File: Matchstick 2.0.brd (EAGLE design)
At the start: 73 x 38 mm, 13 parts, among them IC1 74HCT125D, J1 694106301002, J2 TARGET, J3 691241510006, J4 691241510006, U1 M5STAMP PICO

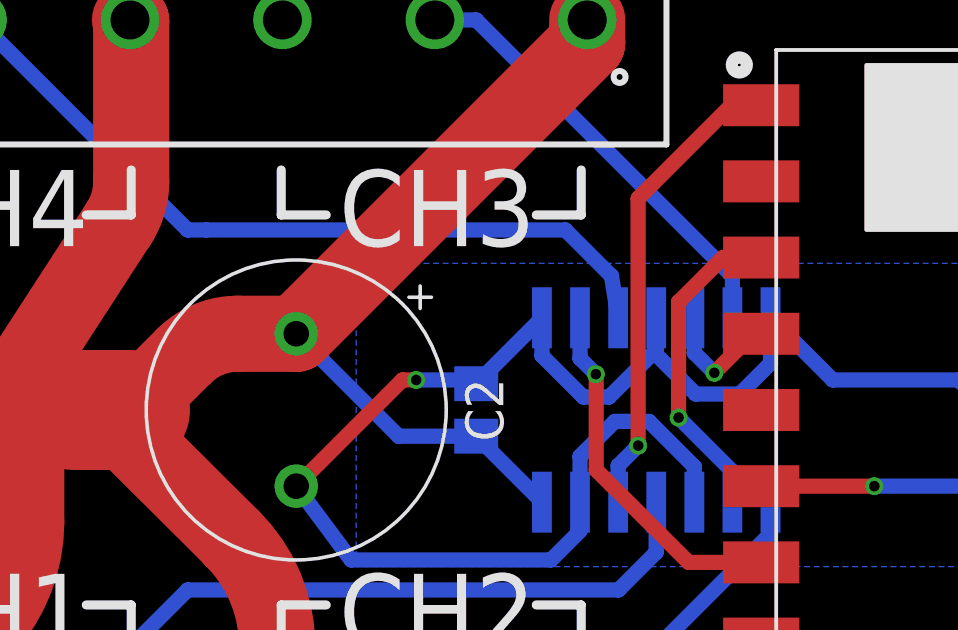
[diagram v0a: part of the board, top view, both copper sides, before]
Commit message: fix few alignment issues
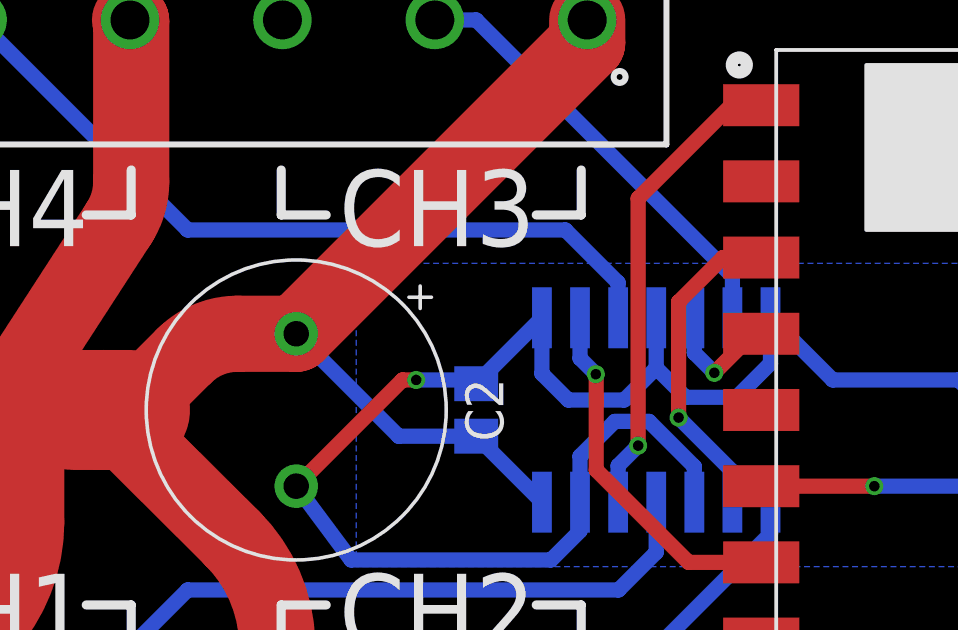
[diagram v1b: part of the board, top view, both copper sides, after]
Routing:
- net GND: track 67.9 -> 67.3 mm
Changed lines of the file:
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@@
 <grid distance="1" unitdist="mm" unit="mm" style="lines" multiple="1" display="yes" altdistance="0.1" altunitdist="mm" altunit="mm"/>
 <layers>
-<layer number="1" name="Top" color="4" fill="1" visible="no" active="yes"/>
+<layer number="1" name="Top" color="4" fill="1" visible="yes" active="yes"/>
 <layer number="16" name="Bottom" color="1" fill="1" visible="yes" active="yes"/>
 <layer number="17" name="Pads" color="2" fill="1" visible="yes" active="yes"/>
@@
 <layer number="19" name="Unrouted" color="6" fill="1" visible="yes" active="yes"/>
 <layer number="20" name="Dimension" color="24" fill="1" visible="yes" active="yes"/>
-<layer number="21" name="tPlace" color="7" fill="1" visible="no" active="yes"/>
+<layer number="21" name="tPlace" color="7" fill="1" visible="yes" active="yes"/>
 <layer number="22" name="bPlace" color="7" fill="1" visible="yes" active="yes"/>
-<layer number="23" name="tOrigins" color="15" fill="1" visible="no" active="yes"/>
+<layer number="23" name="tOrigins" color="15" fill="1" visible="yes" active="yes"/>
 <layer number="24" name="bOrigins" color="15" fill="1" visible="yes" active="yes"/>
-<layer number="25" name="tNames" color="7" fill="1" visible="no" active="yes"/>
+<layer number="25" name="tNames" color="7" fill="1" visible="yes" active="yes"/>
 <layer number="26" name="bNames" color="7" fill="1" visible="yes" active="yes"/>
 <layer number="27" name="tValues" color="7" fill="1" visible="no" active="yes"/>
@@
 <layer number="37" name="tTest" color="7" fill="1" visible="no" active="yes"/>
 <layer number="38" name="bTest" color="7" fill="1" visible="no" active="yes"/>
-<layer number="39" name="tKeepout" color="4" fill="11" visible="no" active="yes"/>
+<layer number="39" name="tKeepout" color="4" fill="11" visible="yes" active="yes"/>
 <layer number="40" name="bKeepout" color="1" fill="11" visible="yes" active="yes"/>
-<layer number="41" name="tRestrict" color="4" fill="10" visible="no" active="yes"/>
+<layer number="41" name="tRestrict" color="4" fill="10" visible="yes" active="yes"/>
 <layer number="42" name="bRestrict" color="1" fill="10" visible="yes" active="yes"/>
 <layer number="43" name="vRestrict" color="2" fill="10" visible="no" active="yes"/>
@@
 <layer number="49" name="Reference" color="7" fill="1" visible="no" active="yes"/>
 <layer number="50" name="dxf" color="7" fill="1" visible="no" active="no"/>
-<layer number="51" name="tDocu" color="7" fill="1" visible="no" active="yes"/>
+<layer number="51" name="tDocu" color="7" fill="1" visible="yes" active="yes"/>
 <layer number="52" name="bDocu" color="7" fill="1" visible="yes" active="yes"/>
 <layer number="53" name="tGND_GNDA" color="7" fill="9" visible="no" active="no"/>
@@
 <wire x1="32.762" y1="18.619" x2="34.27" y2="17.111" width="0.508" layer="16"/>
 <wire x1="34.27" y1="17.111" x2="34.27" y2="15.9266" width="0.508" layer="16"/>
-<wire x1="29.19" y1="22.0734" x2="29.19" y2="20.81" width="0.508" layer="16"/>
-<wire x1="29.19" y1="20.81" x2="30.569" y2="19.431" width="0.508" layer="16"/>
-<wire x1="30.569" y1="19.431" x2="31.431" y2="19.431" width="0.508" layer="16"/>
-<wire x1="31.431" y1="19.431" x2="33" y2="21" width="0.508" layer="16"/>
-<wire x1="33" y1="21" x2="33" y2="22.0734" width="0.508" layer="16"/>
+<wire x1="29.19" y1="20.21" x2="30.069" y2="19.331" width="0.508" layer="16"/>
+<wire x1="30.069" y1="19.331" x2="31.931" y2="19.331" width="0.508" layer="16"/>
+<wire x1="33" y1="20.4" x2="31.931" y2="19.331" width="0.508" layer="16"/>
 <wire x1="27" y1="19.8754" x2="29.19" y2="22.0654" width="0.508" layer="16"/>
 <wire x1="29.19" y1="22.0654" x2="29.19" y2="22.0734" width="0.508" layer="16"/>
@@
 <wire x1="26.8754" y1="20" x2="27" y2="19.8754" width="0.508" layer="16"/>
 <wire x1="36.81" y1="20.554" x2="36.81" y2="22.0734" width="0.508" layer="16"/>
-<wire x1="33" y1="22.0734" x2="33" y2="20.848" width="0.508" layer="16"/>
-<wire x1="34.3184" y1="19.5296" x2="35.7856" y2="19.5296" width="0.508" layer="16"/>
-<wire x1="33" y1="20.848" x2="34.3184" y2="19.5296" width="0.508" layer="16"/>
-<wire x1="35.7856" y1="19.5296" x2="36.81" y2="20.554" width="0.508" layer="16"/>
 <polygon width="1.27" layer="16" isolate="1.016">
 <vertex x="0" y="24"/>
@@
 <vertex x="0" y="14"/>
 </polygon>
+<wire x1="35.678" y1="19.422" x2="36.81" y2="20.554" width="0.508" layer="16"/>
+<wire x1="29.19" y1="22.0734" x2="29.19" y2="20.21" width="0.508" layer="16"/>
+<wire x1="33" y1="22.0734" x2="33" y2="20.4" width="0.508" layer="16"/>
+<wire x1="33" y1="20.4" x2="33.978" y2="19.422" width="0.508" layer="16"/>
+<wire x1="33.978" y1="19.422" x2="35.678" y2="19.422" width="0.508" layer="16"/>
 </signal>
 <signal name="DATA$4">
@@
 <contactref element="J4" pad="5"/>
 <contactref element="IC1" pad="3"/>
-<wire x1="31.73" y1="22.0734" x2="31.51" y2="23.4633375" width="0.508" layer="16"/>
-<wire x1="31.51" y1="23.4633375" x2="29.9733375" y2="25" width="0.508" layer="16"/>
-<wire x1="29.9733375" y1="25" x2="18" y2="25" width="0.508" layer="16"/>
+<wire x1="29.9733375" y1="25" x2="17.38" y2="25" width="0.508" layer="16"/>
 <wire x1="10.38" y1="32" x2="17.38" y2="25" width="0.508" layer="16"/>
-<wire x1="17.38" y1="25" x2="18" y2="25" width="0.508" layer="16"/>
+<wire x1="31.73" y1="22.0734" x2="31.73" y2="23.2433375" width="0.508" layer="16"/>
+<wire x1="31.73" y1="23.2433375" x2="29.9733375" y2="25" width="0.508" layer="16"/>
 </signal>
 <signal name="DI$1">

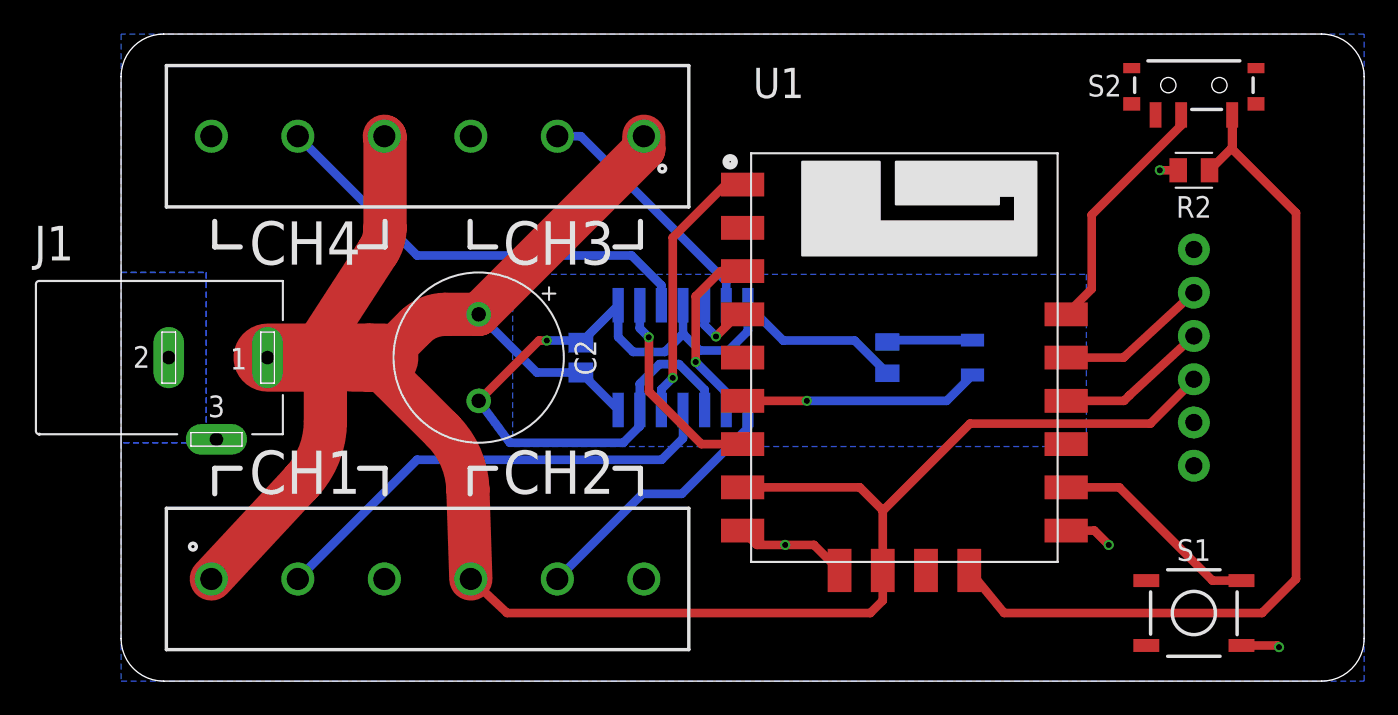
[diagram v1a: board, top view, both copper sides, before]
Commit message: changed signal traces to 0.254mm
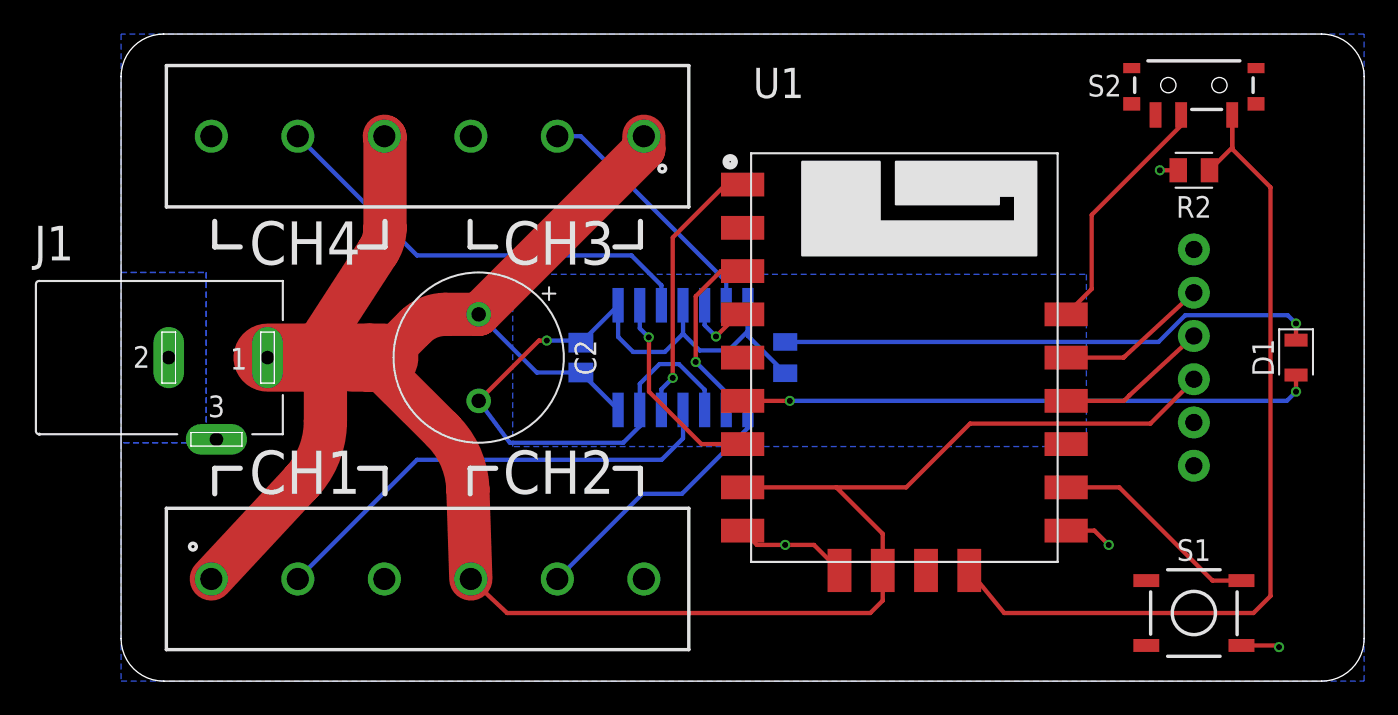
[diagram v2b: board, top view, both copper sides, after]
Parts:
- moved D1 19.0 mm to (69.0, 19.0), flipped to the top
- moved R1 6.00 mm to (39.0, 19.0)
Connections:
- net GND renamed STATUS_LED$2
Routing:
- net SATUS_LED$2: track 5.04 -> 31.8 mm, vias 0 -> 1
- net SATUS_LED$1: track 14.1 -> 33.7 mm, vias 1 -> 2
- net STATUS_LED$2: track 67.3 -> 62.4 mm
- net SW: track 53.8 -> 52.3 mm
- net VCC: track 143.9 -> 145.2 mm
